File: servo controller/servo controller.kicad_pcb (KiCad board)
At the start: 4 copper layers, 30 parts, among them J1 Conn_02x05_Odd_Even, J2 Conn_01x03, J3 Conn_01x03, J4 Conn_01x03, Q1 BC337, Q2 BC337, Q3 BC337, Q4 BC337, Q5 BC337, Q6 BC337, U2 L7805

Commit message: Updates to flex parts and controller
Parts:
- moved R1 12.7 mm to (96.5, 81.3)
- moved R2 12.7 mm to (96.5, 83.8)
- moved R3 12.7 mm to (96.5, 86.4)
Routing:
- net GND: track 122.5 -> 148.6 mm
- net Net-(J4-Pin_3): track 81.7 -> 68.1 mm
- net Net-(J3-Pin_3): track 51.9 -> 40.7 mm
- net Net-(J2-Pin_3): track 45.9 -> 34.7 mm

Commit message: Controller schematic updates for power enable
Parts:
- added Q7: PMOS, Package_TO_SOT_THT:TO-220-3_Vertical, F.Cu at (114.3, 91.4)
- added Q8: BC337, Package_TO_SOT_THT:TO-92_Inline_Wide, F.Cu at (119.4, 83.8)
- added R16: 10k, Resistor_THT:R_Axial_DIN0207_L6.3mm_D2.5mm_P10.16mm_Horizontal, F.Cu at (111.8, 78.7)
- added R17: 1k, Resistor_THT:R_Axial_DIN0207_L6.3mm_D2.5mm_P10.16mm_Horizontal, F.Cu at (127.0, 73.7)
- Q1, Q2, Q3, Q4, Q5, Q6: footprint Package_TO_SOT_THT:TO-92_Inline -> Package_TO_SOT_THT:TO-92_Inline_Wide
- moved Q4 3.59 mm to (104.1, 55.9)
- moved Q5 3.59 mm to (109.2, 66.0), turned to 90 degrees
- moved Q2 3.59 mm to (91.4, 55.9)
- moved Q6 2.54 mm to (106.7, 55.9)
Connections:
- C1 pad 1: +12V -> Net-(Q7-D)
- J1 pad 9: unconnected-(J1-Pin_9-Pad9) -> /SERVO_ENA
- U2 pad 1: +12V -> Net-(Q7-D)
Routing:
- net +12V: track 48.2 -> 90.4 mm, vias 0 -> 4
- net Net-(Q7-D): track 0.00 -> 41.5 mm, vias 0 -> 3
- net /SCL: track 61.9 -> 77.1 mm, vias 0 -> 1
- net +3.3V: track 81.2 -> 96.2 mm, vias 0 -> 4
- net Net-(Q7-G): track 0.00 -> 14.8 mm
- net /SERVO_ENA: track 0.00 -> 13.8 mm
- net /SERVO_2_5V: track 26.4 -> 35.8 mm, vias 0 -> 1
- net Net-(Q8-B): track 0.00 -> 5.97 mm
- net /SDA: track 72.6 -> 78.2 mm, vias 0 -> 1
- net /SERVO_1_5V: track 34.4 -> 39.7 mm, vias 0 -> 2
- net Net-(Q5-C): track 17.4 -> 13.6 mm
- net Net-(Q1-C): track 14.8 -> 11.1 mm
- net Net-(Q4-B): track 11.7 -> 15.4 mm, vias 0 -> 1
- net /SERVO_0_5V: track 26.8 -> 30.4 mm
- net GND: track 148.6 -> 151.7 mm
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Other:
- board outline added: 50.8 x 45.7 mm
- copper layers 4 -> 2

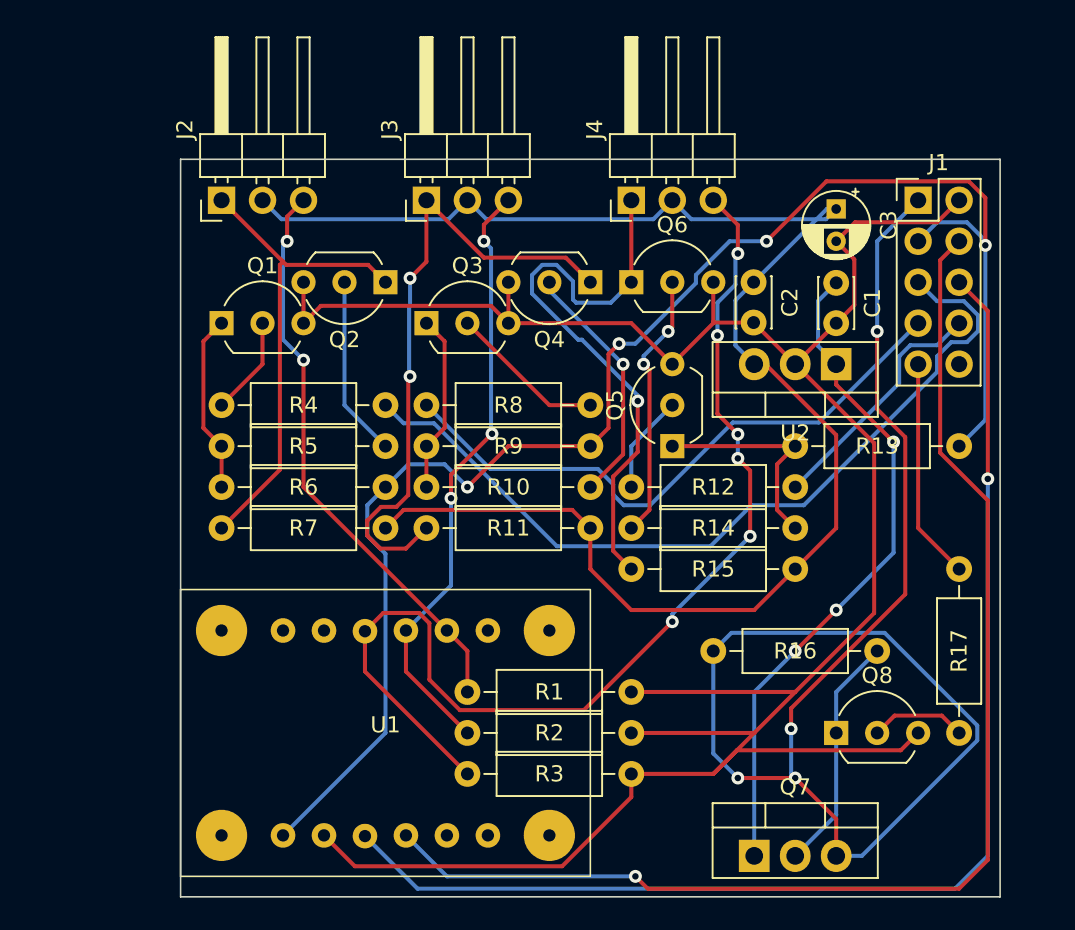
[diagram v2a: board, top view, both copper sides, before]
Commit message: Controller schematic fixes and new grasper concept
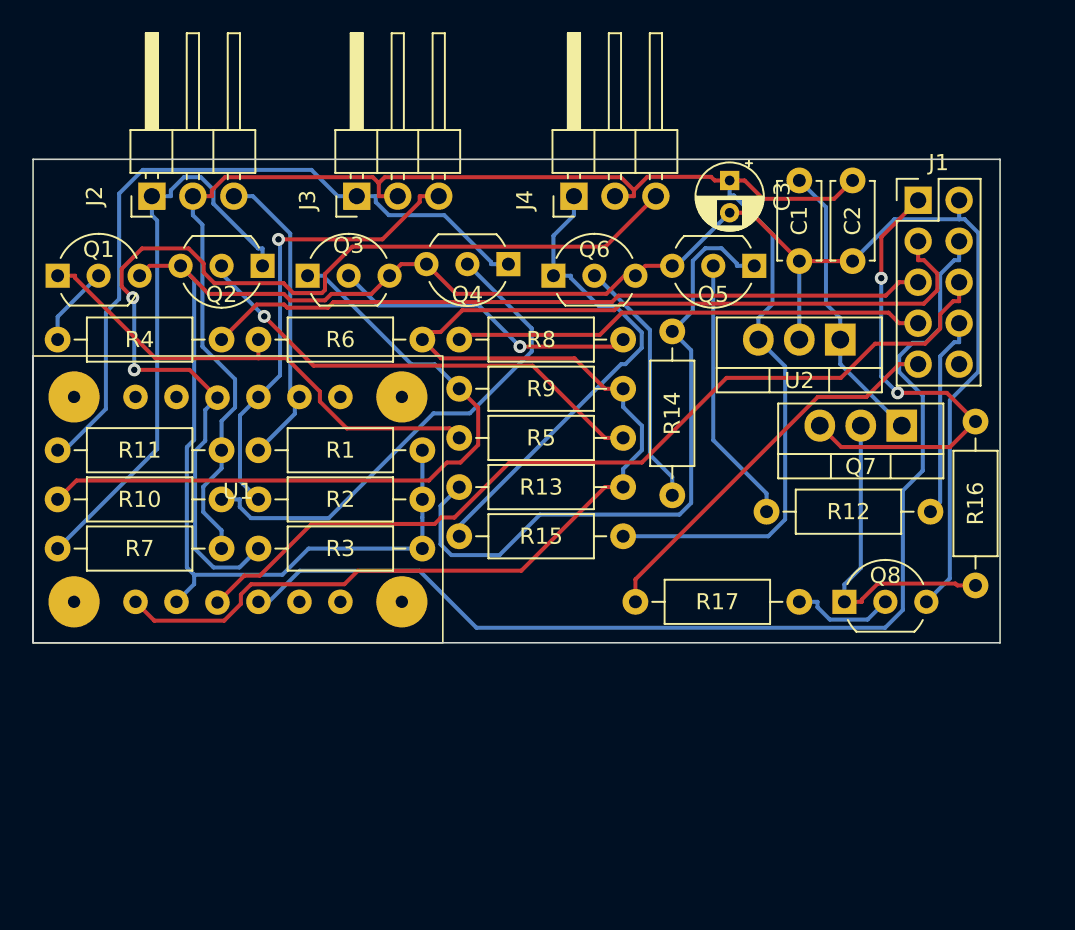
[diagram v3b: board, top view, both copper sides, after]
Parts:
- C1, C2: footprint Capacitor_THT:C_Disc_D3.0mm_W2.0mm_P2.50mm -> Capacitor_THT:C_Disc_D4.7mm_W2.5mm_P5.00mm
- moved Q7 28.2 mm to (123.4, 64.8), turned to 180 degrees
- moved R11 23.4 mm to (71.1, 66.3)
- moved R10 22.9 mm to (71.1, 69.3)
- moved R16 21.6 mm to (128.0, 64.5), turned to -90 degrees
- moved R13 21.0 mm to (96.0, 68.6)
- moved R17 20.2 mm to (106.9, 75.7), turned to 0 degrees
- moved R1 19.8 mm to (83.6, 66.3)
- moved R2 19.4 mm to (83.6, 69.3)
- moved R3 19.1 mm to (83.6, 72.4)
- moved U1 17.1 mm to (82.3, 69.3)
- moved R5 14.7 mm to (96.0, 65.5)
- moved R14 14.4 mm to (109.2, 58.9), turned to -90 degrees
- moved Q5 12.3 mm to (114.3, 54.9), turned to 180 degrees
- moved R4 10.9 mm to (81.3, 59.4)
- moved R15 10.9 mm to (96.0, 71.6)
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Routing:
- net +12V: track 90.4 -> 29.7 mm, vias 4 -> 2
- net Net-(Q3-C): track 11.1 -> 43.8 mm
- net Net-(Q5-C): track 13.6 -> 41.9 mm
- net Net-(Q7-D): track 41.5 -> 17.8 mm, vias 3 -> 0
- net /SCL: track 77.1 -> 55.4 mm, vias 1 -> 0
- net Net-(Q1-C): track 11.1 -> 30.7 mm
- net GND: track 151.7 -> 132.7 mm
- net Net-(Q2-B): track 11.2 -> 29.6 mm, vias 0 -> 1
- net Net-(J2-Pin_3): track 35.7 -> 19.2 mm, vias 2 -> 0
- net Net-(Q4-B): track 15.4 -> 31.3 mm, vias 1 -> 0
- net /SERVO_ENA: track 13.8 -> 24.4 mm
- net Net-(Q5-B): track 6.13 -> 16.6 mm
- net /SDA: track 78.2 -> 68.8 mm, vias 1 -> 0
- net Net-(Q3-B): track 9.72 -> 19.0 mm, vias 0 -> 1
- net Net-(J3-Pin_3): track 37.6 -> 28.9 mm, vias 3 -> 1
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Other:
- board size 50.8 x 45.7 mm -> 59.9 x 30 mm

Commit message: Add servo controller electrical changes
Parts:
- added C4: 4.7nF, Capacitor_THT:C_Disc_D4.7mm_W2.5mm_P5.00mm, F.Cu at (93.8, 52.6)
- added C5: 4.7nF, Capacitor_THT:C_Disc_D4.7mm_W2.5mm_P5.00mm, F.Cu at (112.3, 67.9)
- added C6: 4.7nF, Capacitor_THT:C_Disc_D4.7mm_W2.5mm_P5.00mm, F.Cu at (71.2, 52.6)
- renumbered R1 to R1+C7, R2 to R2+C8, R3 to R3+C9
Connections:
- J1 pad 10: unconnected-(J1-Pin_10-Pad10) -> /SERVO_ENA
- J1 pad 9: /SERVO_ENA -> unconnected-(J1-Pin_9-Pad9)
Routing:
- net Net-(J4-Pin_3): track 65.5 -> 117.5 mm
- net /SERVO_ENA: track 24.4 -> 39.7 mm
- net /SERVO_2_5V: track 29.9 -> 40.7 mm, vias 0 -> 3
- net Net-(J2-Pin_3): track 19.2 -> 25.9 mm
- net /SERVO_0_5V: track 35.5 -> 42.2 mm
- net Net-(J3-Pin_3): track 28.9 -> 33.8 mm
- net /SERVO_1_5V: track 45.2 -> 46.2 mm
